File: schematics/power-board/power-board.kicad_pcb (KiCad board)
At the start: 2 copper layers, 125 x 72.5 mm, 23 parts, among them J1 5V, J2 5V, J3 +12V, J4 +12V, J5 -12V, J6 -12V, J7 GND, J8 Conn_01x01_Socket, J9 5V, Q1 BT151-500R, U1 USBC Module, U2 TPS5430 Module 5V, U3 TPS5430 Module 12V

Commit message: fix: move vias to back plane
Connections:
- U1 pad 1: Net-(SW1-B) -> /VIN
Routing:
- net /VIN: track 36.7 -> 24.2 mm

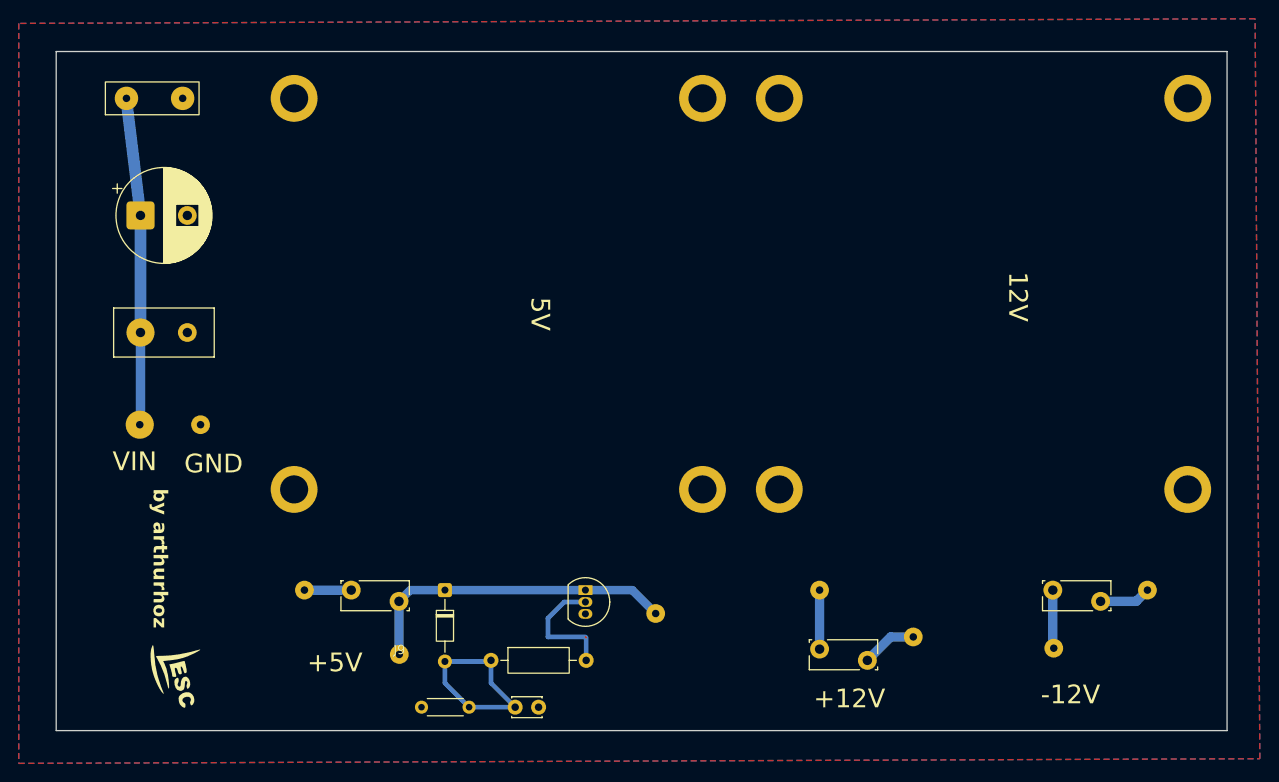
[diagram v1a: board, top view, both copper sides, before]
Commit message: refactor: fix PCBBox holes dimensions and remake pcb vias with the new components
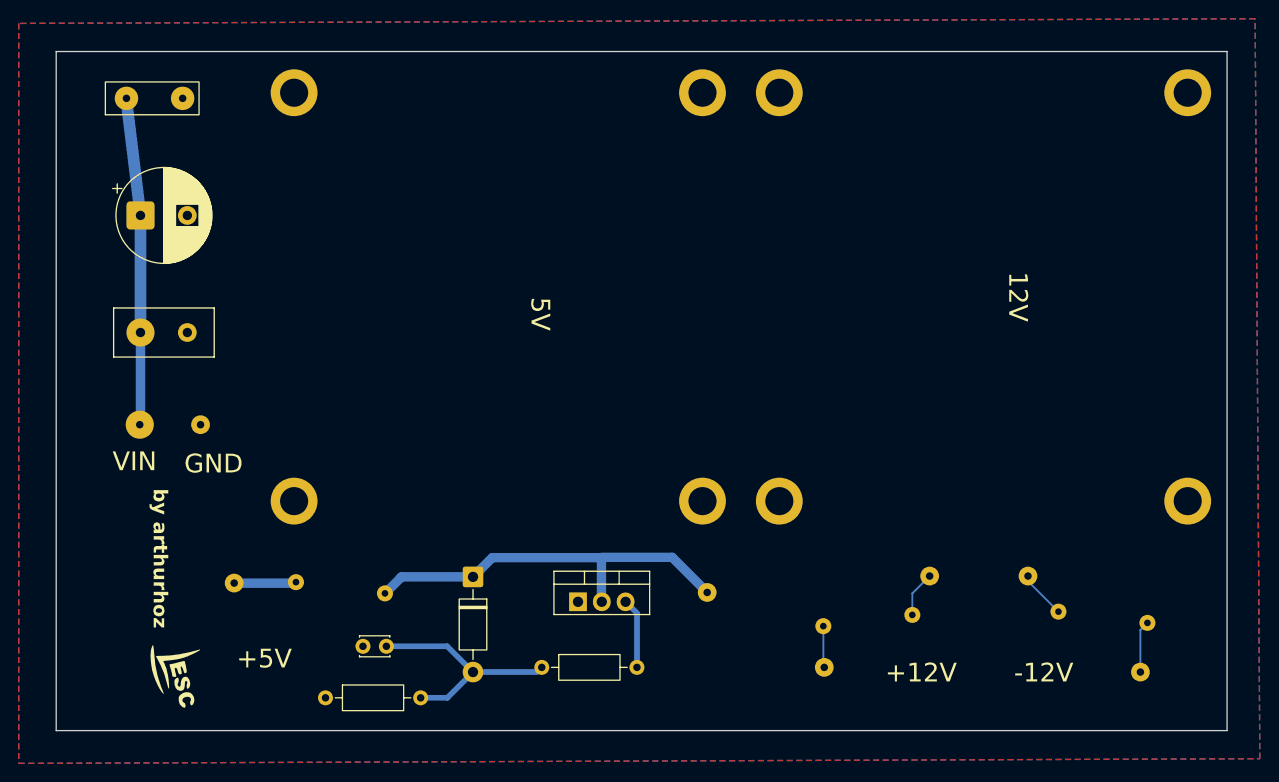
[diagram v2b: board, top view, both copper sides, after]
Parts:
- removed the F1 at (120.0, 75.0)
- removed F2, F3: RXEF110 1A1, Fuse:Fuse_Bourns_MF-RG300
- removed J9: 5V, footprints:Connector
- added F1: Fuse, Fuse:Fuse_Bourns_MF-RHT200, F.Cu at (115.8, 74.2)
- added F1: Fuse, Fuse:Fuse_Bourns_MF-RHT200, F.Cu at (197.2, 77.3)
- added F1: Fuse, Fuse:Fuse_Bourns_MF-RHT200, B.Cu at (178.2, 77.7)
- D1: footprint Diode_THT:D_DO-34_SOD68_P7.62mm_Horizontal -> Diode_THT:D_DO-41_SOD81_P10.16mm_Horizontal
- Q1: footprint Package_TO_SOT_THT:TO-92_Inline -> Package_TO_SOT_THT:TO-220-3_Vertical
- R1: footprint Resistor_THT:R_Axial_DIN0204_L3.6mm_D1.6mm_P5.08mm_Horizontal -> Resistor_THT:R_Axial_DIN0207_L6.3mm_D2.5mm_P10.16mm_Horizontal
- moved C4 15.2 mm to (123.8, 81.0), turned to 180 degrees
- moved J5 12.8 mm to (192.2, 73.5)
- moved J3 11.8 mm to (181.8, 73.5)
- moved R1 10.3 mm to (117.2, 86.5)
- moved J4 10.0 mm to (170.5, 83.2)
- moved J6 9.60 mm to (204.2, 83.8)
- moved J1 7.54 mm to (107.5, 74.2)
- moved J2 5.94 mm to (158.0, 75.2)
- moved R2 5.47 mm to (140.3, 83.2)
- moved D1 3.31 mm to (133.0, 73.6)
- moved Q1 1.48 mm to (144.2, 76.2), turned to 0 degrees
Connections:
- J3 pad 1: Net-(J3-Pin_1) -> /+12V
- J5 pad 1: Net-(J5-Pin_1) -> /-12V
- Q1 pad 1: /5V -> GND
- Q1 pad 2: Net-(Q1-G) -> /5V
- Q1 pad 3: GND -> Net-(Q1-G)
- U1 pad 1: /VIN -> Net-(SW1-B)
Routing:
- net /5V: track 34.6 -> 42.3 mm
- net Net-(J3-Pin_1): track 6.30 -> 0.00 mm
- net Net-(Q1-G): track 13.2 -> 7.50 mm
- net Net-(J5-Pin_1): track 5.50 -> 0.00 mm
- net /-12V: track 6.24 -> 10.8 mm
- net /+12V: track 5.94 -> 9.36 mm
- net Net-(D1-A): track 21.9 -> 24.7 mm
- net Net-(J1-Pin_1): track 5.00 -> 6.64 mm
